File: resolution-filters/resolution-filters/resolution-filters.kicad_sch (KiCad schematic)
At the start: 64 parts, among them J501 Conn_Coaxial, J502 Terminal Block, J503 Conn_Coaxial, K501 G5V-1, K502 G5V-1, SW501 SW_SPST, T501 Transformer_1P_1S, T502 Transformer_1P_1S, Y501 10.7MHz, Y502 10.7MHz, Y503 10.7MHz, Y504 10.7MHz

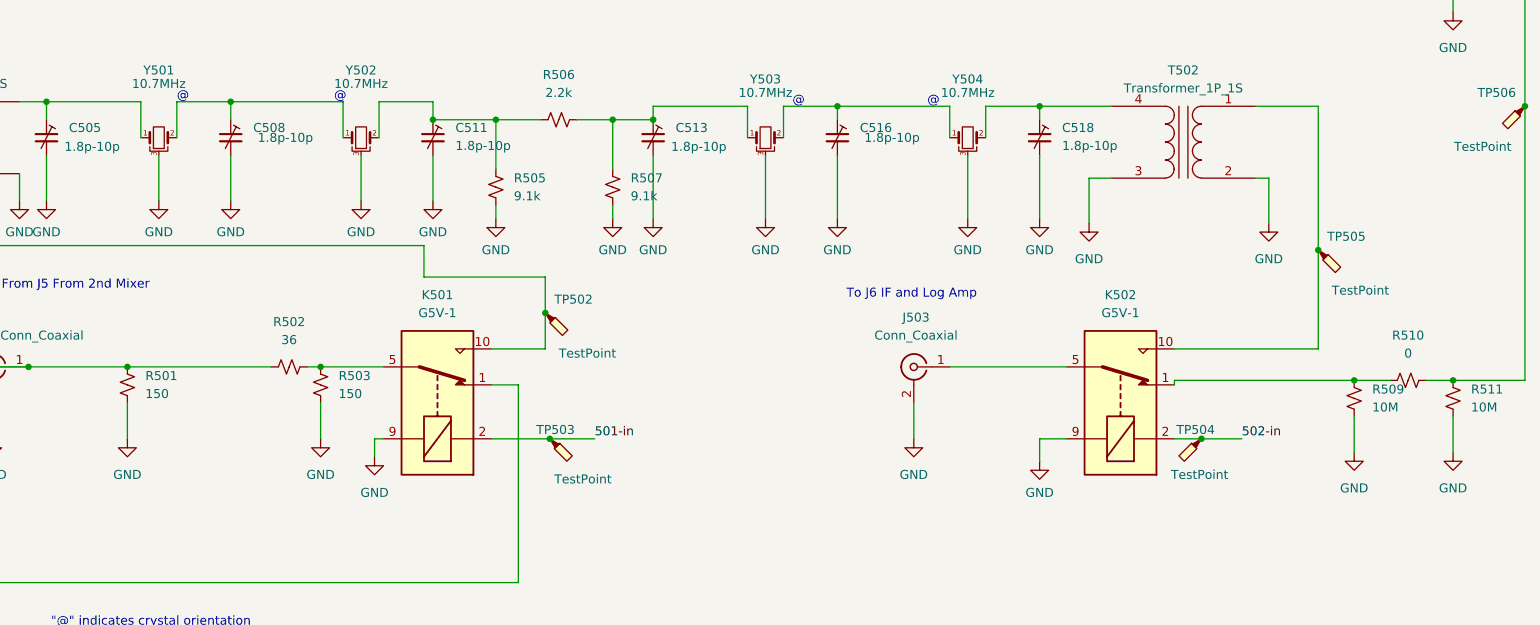
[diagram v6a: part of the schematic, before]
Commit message: Fix POS200 footprint and Terminal Block footprint of VCO 1st Mixer Board.  Rev 1.
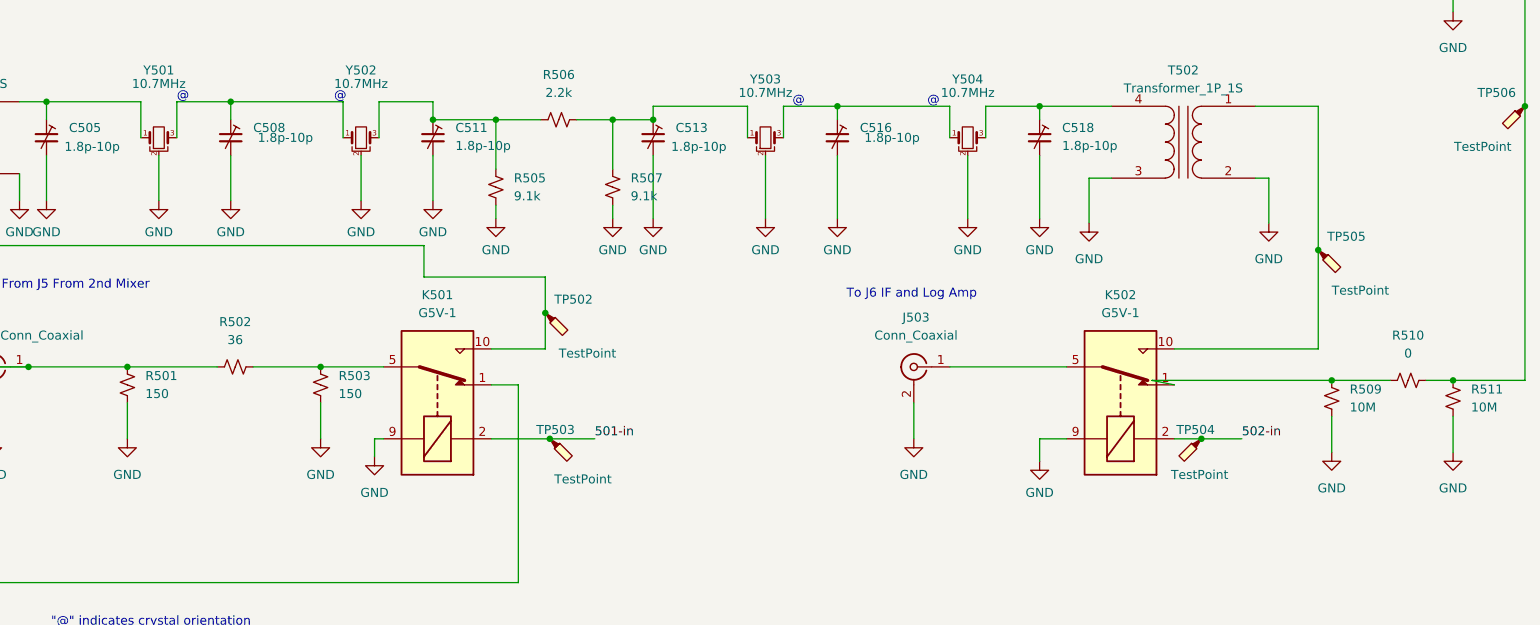
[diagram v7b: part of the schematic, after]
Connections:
- net GND: now also Y501.2, Y502.2, Y503.2, Y504.2; no longer Y501.3, Y502.3, Y503.3, Y504.3
- net at C511.1, R505.1, R506.1: now also Y502.3; no longer Y502.2
- net at C518.1, T502.4 (SB): now also Y504.3; no longer Y504.2
- net at C508.1, Y502.1: now also Y501.3; no longer Y501.2
- net at C516.1, Y504.1: now also Y503.3; no longer Y503.2
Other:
- moved on the sheet: R502, R509
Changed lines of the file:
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@@
   (junction (at 53.34 61.595) (diameter 0) (color 0 0 0 0)
   )
-  (junction (at 238.76 152.4) (diameter 0) (color 0 0 0 0)
+  (junction (at 235.585 152.4) (diameter 0) (color 0 0 0 0)
   )
   (junction (at 252.73 77.47) (diameter 0) (color 0 0 0 0)
@@
     (stroke (width 0) (type default) (color 0 0 0 0))
   )
-  (wire (pts (xy 213.36 152.4) (xy 213.36 153.035))
+  (wire (pts (xy 210.185 152.4) (xy 213.36 153.035))
     (stroke (width 0) (type default) (color 0 0 0 0))
   )
@@
     (stroke (width 0) (type default) (color 0 0 0 0))
   )
-  (wire (pts (xy 85.725 150.495) (xy 65.405 150.495))
+  (wire (pts (xy 78.105 150.495) (xy 65.405 150.495))
     (stroke (width 0) (type default) (color 0 0 0 0))
   )
@@
     (stroke (width 0) (type default) (color 0 0 0 0))
   )
-  (wire (pts (xy 92.71 150.495) (xy 90.805 150.495))
-    (stroke (width 0) (type default) (color 0 0 0 0))
-  )
-  (wire (pts (xy 213.36 152.4) (xy 238.76 152.4))
+  (wire (pts (xy 92.71 150.495) (xy 83.185 150.495))
+    (stroke (width 0) (type default) (color 0 0 0 0))
+  )
+  (wire (pts (xy 210.185 152.4) (xy 235.585 152.4))
     (stroke (width 0) (type default) (color 0 0 0 0))
   )
@@
     (stroke (width 0) (type default) (color 0 0 0 0))
   )
-  (wire (pts (xy 243.84 152.4) (xy 238.76 152.4))
+  (wire (pts (xy 235.585 152.4) (xy 243.84 152.4))
     (stroke (width 0) (type default) (color 0 0 0 0))
   )
@@
     (stroke (width 0) (type default) (color 0 0 0 0))
   )
-  (wire (pts (xy 238.76 157.48) (xy 238.76 162.56))
+  (wire (pts (xy 235.585 157.48) (xy 235.585 162.56))
     (stroke (width 0) (type default) (color 0 0 0 0))
   )
@@
     (pin "1")
   )
-  (symbol (lib_id "Device:R_Small_US") (at 238.76 154.94 0) (unit 1)
-    (in_bom yes) (on_board yes) (fields_autoplaced)
-    (property "Reference" "R509" (id 0) (at 241.3 153.6699 0)
-      (effects (font (size 1.27 1.27)) (justify left))
-    )
-    (property "Value" "10M" (id 1) (at 241.3 156.2099 0)
-      (effects (font (size 1.27 1.27)) (justify left))
-    )
-    (property "Footprint" "Resistor_THT:R_Axial_DIN0207_L6.3mm_D2.5mm_P7.62mm_Horizontal" (id 2) (at 238.76 154.94 0)
-      (effects (font (size 1.27 1.27)) hide)
-    )
-    (property "Datasheet" "https://www.yageo.com/upload/media/product/productsearch/datasheet/lr/YAGEO%20RSF_datasheet_2021v0.pdf" (id 3) (at 238.76 154.94 0)
+  (symbol (lib_id "Device:R_Small_US") (at 235.585 154.94 0) (unit 1)
+    (in_bom yes) (on_board yes) (fields_autoplaced)
+    (property "Reference" "R509" (id 0) (at 238.125 153.6699 0)
+      (effects (font (size 1.27 1.27)) (justify left))
+    )
+    (property "Value" "10M" (id 1) (at 238.125 156.2099 0)
+      (effects (font (size 1.27 1.27)) (justify left))
+    )
+    (property "Footprint" "Resistor_THT:R_Axial_DIN0207_L6.3mm_D2.5mm_P7.62mm_Horizontal" (id 2) (at 235.585 154.94 0)
+      (effects (font (size 1.27 1.27)) hide)
+    )
+    (property "Datasheet" "https://www.yageo.com/upload/media/product/productsearch/datasheet/lr/YAGEO%20RSF_datasheet_2021v0.pdf" (id 3) (at 235.585 154.94 0)
       (effects (font (size 1.27 1.27)) hide)
     )
@@
     (pin "1")
   )
-  (symbol (lib_id "Device:Crystal_GND3_Small") (at 155.575 118.11 0) (unit 1)
+  (symbol (lib_name "Crystal_GND3_Small_2") (lib_id "Device:Crystal_GND3_Small") (at 155.575 118.11 0) (unit 1)
     (in_bom yes) (on_board yes)
     (property "Reference" "Y503" (id 0) (at 155.575 109.855 0))
@@
       (effects (font (size 1.27 1.27)) hide)
     )
-    (property "Datasheet" "https://www.digikey.com/en/products/detail/ecs-inc/ECS-10-7-7-5B/110031" (id 3) (at 155.575 118.11 0)
+    (property "Datasheet" "~" (id 3) (at 155.575 118.11 0)
       (effects (font (size 1.27 1.27)) hide)
     )
@@
     (pin "1")
   )
-  (symbol (lib_id "Device:Crystal_GND3_Small") (at 184.15 118.11 0) (unit 1)
+  (symbol (lib_name "Crystal_GND3_Small_3") (lib_id "Device:Crystal_GND3_Small") (at 184.15 118.11 0) (unit 1)
     (in_bom yes) (on_board yes)
     (property "Reference" "Y504" (id 0) (at 184.15 109.855 0))
@@
       (effects (font (size 1.27 1.27)) hide)
     )
-    (property "Datasheet" "https://www.digikey.com/en/products/detail/ecs-inc/ECS-10-7-7-5B/110031" (id 3) (at 184.15 118.11 0)
+    (property "Datasheet" "~" (id 3) (at 184.15 118.11 0)
       (effects (font (size 1.27 1.27)) hide)
     )
@@
     (pin "9")
   )
-  (symbol (lib_id "Device:Crystal_GND3_Small") (at 98.425 118.11 0) (unit 1)
+  (symbol (lib_name "Crystal_GND3_Small_1") (lib_id "Device:Crystal_GND3_Small") (at 98.425 118.11 0) (unit 1)
     (in_bom yes) (on_board yes)
     (property "Reference" "Y502" (id 0) (at 98.425 108.585 0))
@@
       (effects (font (size 1.27 1.27)) hide)
     )
-    (property "Datasheet" "https://www.digikey.com/en/products/detail/ecs-inc/ECS-10-7-7-5B/110031" (id 3) (at 98.425 118.11 0)
+    (property "Datasheet" "~" (id 3) (at 98.425 118.11 0)
       (effects (font (size 1.27 1.27)) hide)
     )
@@
       (effects (font (size 1.27 1.27)) hide)
     )
-    (property "Datasheet" "https://www.digikey.com/en/products/detail/ecs-inc/ECS-10-7-7-5B/110031" (id 3) (at 69.85 118.11 0)
+    (property "Datasheet" "~" (id 3) (at 69.85 118.11 0)
       (effects (font (size 1.27 1.27)) hide)
     )
@@
     (pin "2")
   )
-  (symbol (lib_id "Device:R_Small_US") (at 88.265 150.495 90) (unit 1)
-    (in_bom yes) (on_board yes) (fields_autoplaced)
-    (property "Reference" "R502" (id 0) (at 88.265 144.145 90))
-    (property "Value" "36" (id 1) (at 88.265 146.685 90))
-    (property "Footprint" "Resistor_THT:R_Axial_DIN0207_L6.3mm_D2.5mm_P7.62mm_Horizontal" (id 2) (at 88.265 150.495 0)
-      (effects (font (size 1.27 1.27)) hide)
-    )
-    (property "Datasheet" "https://www.yageo.com/upload/media/product/productsearch/datasheet/lr/YAGEO%20RSF_datasheet_2021v0.pdf" (id 3) (at 88.265 150.495 0)
+  (symbol (lib_id "Device:R_Small_US") (at 80.645 150.495 90) (unit 1)
+    (in_bom yes) (on_board yes) (fields_autoplaced)
+    (property "Reference" "R502" (id 0) (at 80.645 144.145 90))
+    (property "Value" "36" (id 1) (at 80.645 146.685 90))
+    (property "Footprint" "Resistor_THT:R_Axial_DIN0207_L6.3mm_D2.5mm_P7.62mm_Horizontal" (id 2) (at 80.645 150.495 0)
+      (effects (font (size 1.27 1.27)) hide)
+    )
+    (property "Datasheet" "https://www.yageo.com/upload/media/product/productsearch/datasheet/lr/YAGEO%20RSF_datasheet_2021v0.pdf" (id 3) (at 80.645 150.495 0)
       (effects (font (size 1.27 1.27)) hide)
     )
@@
     (pin "1")
   )
-  (symbol (lib_id "power:GND") (at 238.76 162.56 0) (unit 1)
-    (in_bom yes) (on_board yes) (fields_autoplaced)
-    (property "Reference" "#PWR0542" (id 0) (at 238.76 168.91 0)
-      (effects (font (size 1.27 1.27)) hide)
-    )
-    (property "Value" "GND" (id 1) (at 238.76 167.64 0))
-    (property "Footprint" "" (id 2) (at 238.76 162.56 0)
-      (effects (font (size 1.27 1.27)) hide)
-    )
-    (property "Datasheet" "" (id 3) (at 238.76 162.56 0)
-      (effects (font (size 1.27 1.27)) hide)
-    )
+  (symbol (lib_id "power:GND") (at 235.585 162.56 0) (unit 1)
+    (in_bom yes) (on_board yes) (fields_autoplaced)
+    (property "Reference" "#PWR0542" (id 0) (at 235.585 168.91 0)
+      (effects (font (size 1.27 1.27)) hide)
+    )
+    (property "Value" "GND" (id 1) (at 235.585 167.64 0))
+    (property "Footprint" "" (id 2) (at 235.585 162.56 0)
+      (effects (font (size 1.27 1.27)) hide)
+    )
+    (property "Datasheet" "" (id 3) (at 235.585 162.56 0)
+      (effects (font (size 1.27 1.27)) hide)
+    )

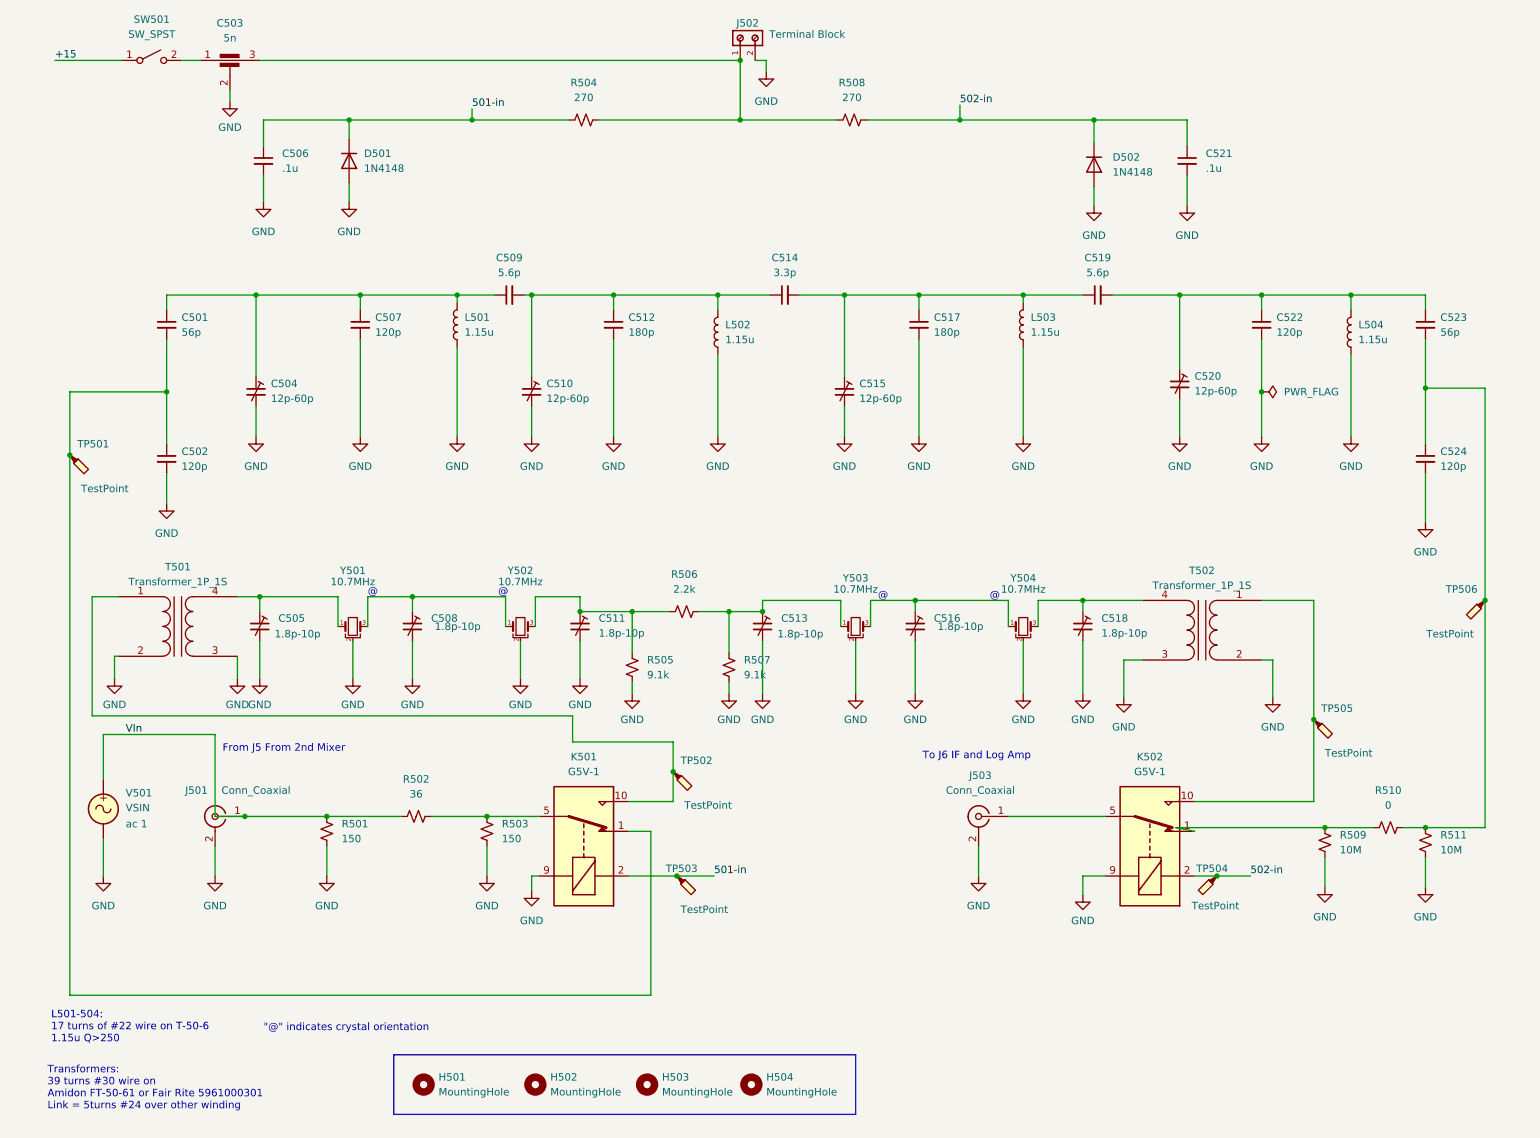
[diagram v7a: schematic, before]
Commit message: corrections to resolution-filters
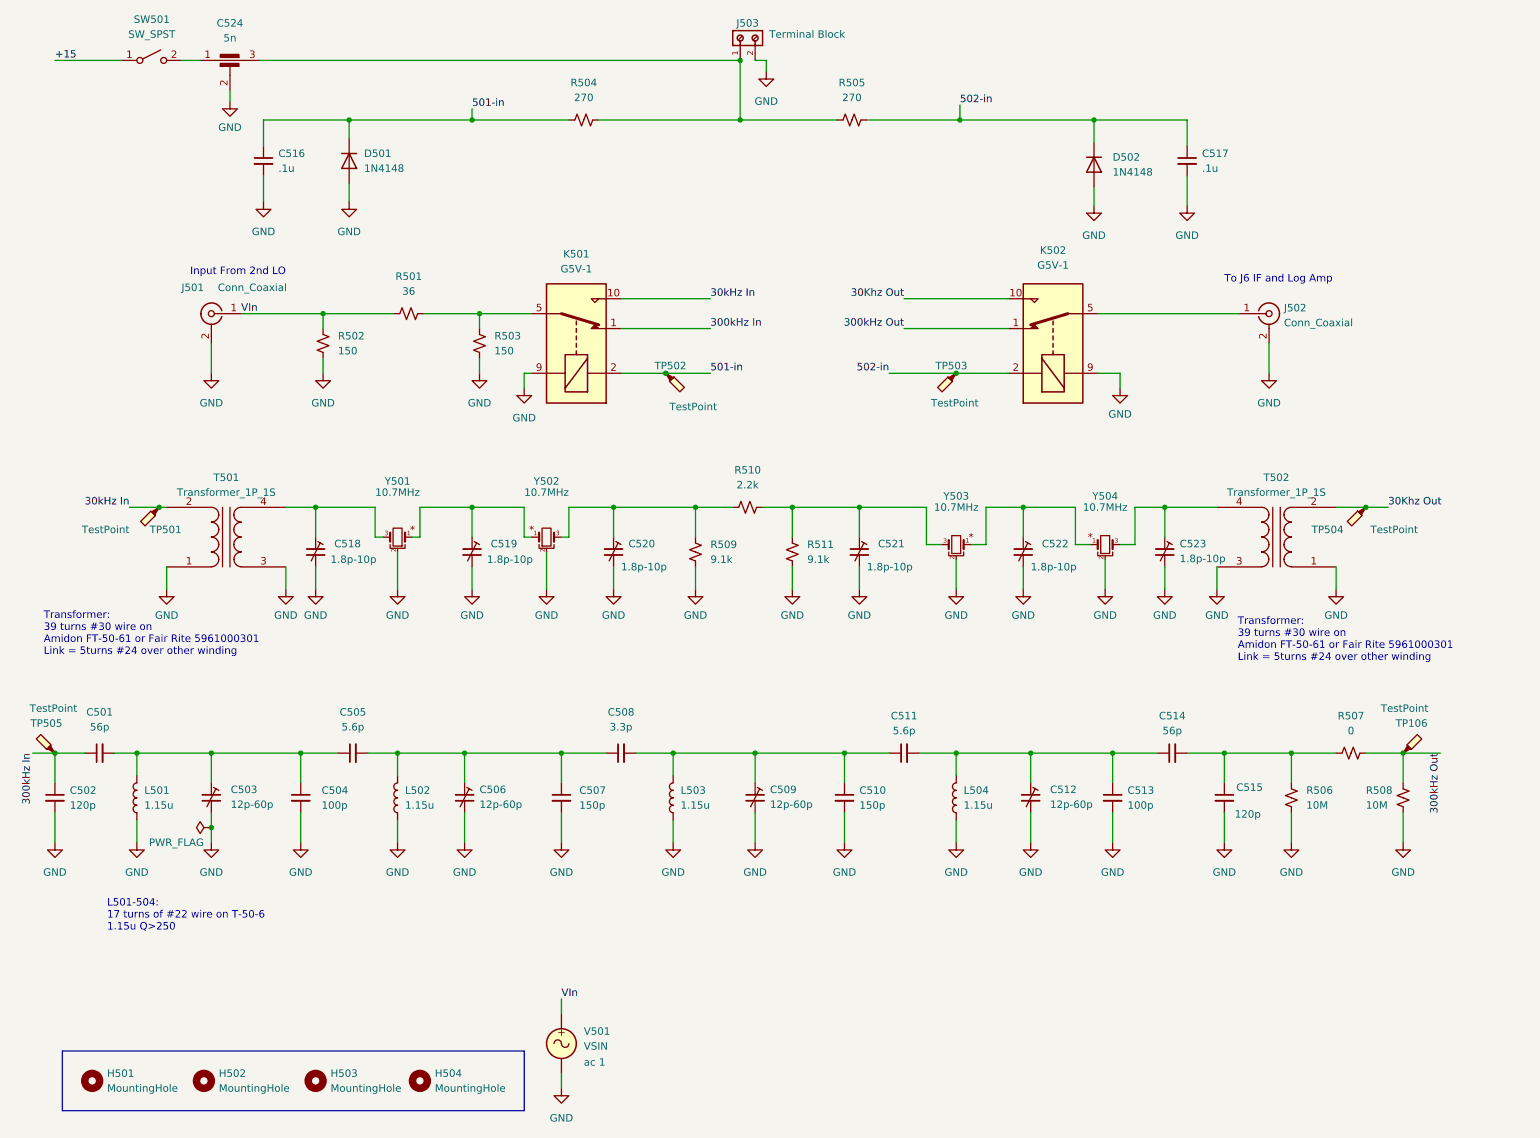
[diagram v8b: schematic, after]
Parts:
- removed TP505: TestPoint, TestPoint:TestPoint_Pad_D2.0mm, symbol Connector:TestPoint_Probe
- added TP106: TestPoint, TestPoint:TestPoint_Pad_D2.0mm, symbol Connector:TestPoint_Probe
- C504: renamed from C507; value 120p -> 100p
- C507: renamed from C512; value 180p -> 150p
- C510: renamed from C517; value 180p -> 150p
- C513: renamed from C522; value 120p -> 100p
- renumbered C504 to C503, C509 to C505, C510 to C506, C514 to C508, C515 to C509, C519 to C511, C520 to C512, C523 to C514, C524 to C515, C506 to C516, C521 to C517, C505 to C518, C508 to C519, C511 to C520, C513 to C521, C516 to C522, C518 to C523, C503 to C524, J503 to J502, J502 to J503, R502 to R501, R501 to R502, R508 to R505, R509 to R506, R510 to R507, R511 to R508, R505 to R509, R506 to R510, R507 to R511, TP502 to TP501, TP503 to TP502, TP504 to TP503, TP506 to TP504, TP501 to TP505
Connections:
- net GND: now also T501.1 (AB), T502.1 (AB); no longer T501.2 (AB), T502.2 (AB)
- net at C503.1, C504.1, C505.1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: now also C501.2; no longer C501.1
- net 30Khz Out: now reaches K502.10
- net 30Khz Out: now also T502.2 (AA), TP504.1; no longer T502.1 (AA)
- net 300kHz In: now reaches C502.1, K501.1, TP505.1
- net 300kHz In: now also C501.1; no longer C501.2
- net at R506.1, R507.1: now also C514.2, C515.1; no longer K502.1
- net at C519.1, Y502.1: now also Y501.1; no longer Y501.3
- net at C521.1, R510.2, R511.1: now also Y503.3; no longer Y503.1
- net at C518.1, T501.4 (SB): now also Y501.3; no longer Y501.1
- net 30kHz In: now reaches K501.10, TP501.1
- net 30kHz In: now also T501.2 (AA); no longer T501.1 (AA)
- net at C522.1, Y504.1: now also Y503.1; no longer Y503.3
- new net 300kHz Out: K502.1, R507.2, R508.1, TP106.1
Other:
- note added: "Input From 2nd LO"
- note added: "Transformer: 39 turns #30 wire on Amidon FT-50-61 or Fair Rite 5961000301 Link = 5turns #24 over other winding"
- note removed: ""@" indicates crystal orientation"
- note removed: "@"
- note removed: "From J5 From 2nd Mixer"
- note removed: "Transformers: 39 turns #30 wire on Amidon FT-50-61 or Fair Rite 5961000301 Link = 5turns #24 over other winding"
- moved on the sheet: C501, C502, C503, C504, C505, C506, C507, C508, C509, C510, C511, C512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
